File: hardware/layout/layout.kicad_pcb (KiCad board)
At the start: 4 copper layers, 60 parts, among them J1 ?, J2 ?, J3 2.54mm 18 x 2 SMD Vertical Fe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, SW1 ?, U1 ?, U2 ?, U3 ?, U4 ?, U5 ?, Y1 ECS-120-12-33Q-JES-TR

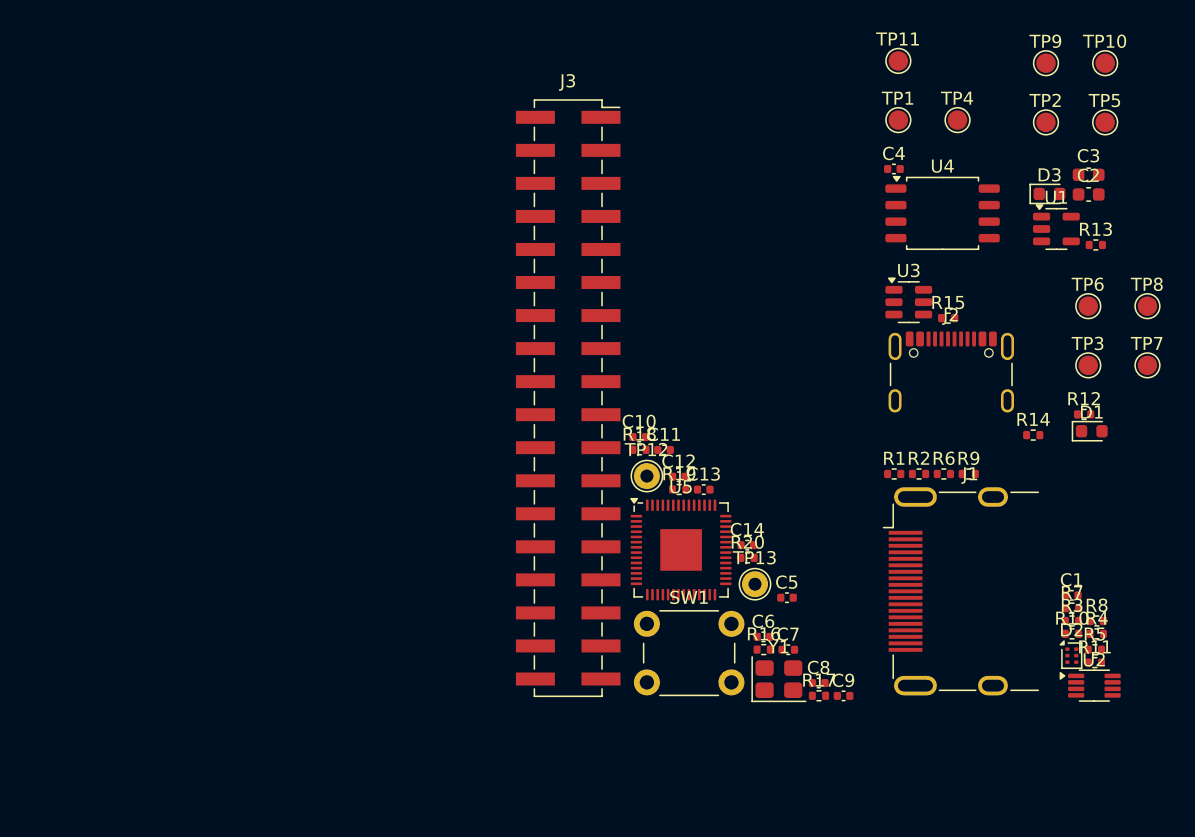
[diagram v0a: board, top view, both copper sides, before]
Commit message: hardware: DRC relaxation pass — 4-layer planes, pours, net classes, cost rules, clean silk
Checkpoint of the bring-up layout before the RP2040-module refactor.

- Planes/pours: In1=GND plane, In2=VDD_3V3 plane, F/B GND pours, GND
  stitch-via grid + QFN exposed-pad thermal vias.
- Resolved real DRC: track/pad clearances (incl. QSPI_IO3<->C7 via a
  small C7 nudge), dangling vias/tracks, starved thermals
  (min_resolved_spokes 2->1), isolated copper.
- Custom rules (layout.kicad_dru): 0.13mm fine-pitch clearance inside
  U2 (PCA9306) and U5 (RP2040 QFN) courtyards.
- Net classes: Power (VDD_*) 0.4mm, USB diff-pair 0.25/0.20mm.
- Project: resolve ${PCB_NAME}/${PCB_VERSION} title-block vars,
  lib_footprint_mismatch -> ignore.
- Silkscreen: hide all reference designators, strip body outlines to
  pin-1 / polarity marks only.
- Plus in-progress signal routing.

DRC: 0 error-severity violations; 38 unconnected remain (off-board
test-point stubs + unfinished on-board routing).
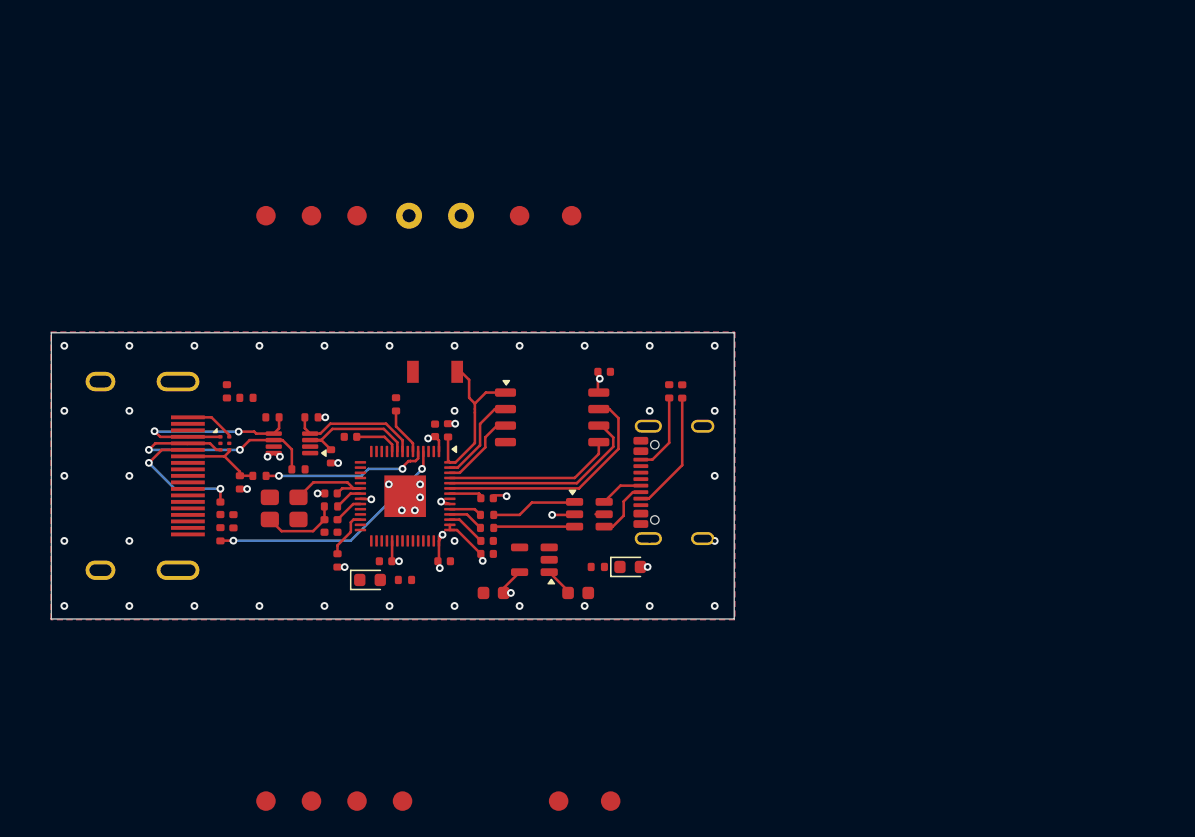
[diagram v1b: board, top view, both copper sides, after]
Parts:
- removed J3: 2.54mm 18 x 2 SMD Vertical Female, kicad_libraries_kicad-footprints_Connector_PinSocket_2.54mm@9.0.3:PinSocket_2x18_P2.54mm_Vertical_SMD
- D2: value ? -> PESD5V0L4UF
- J1: value ? -> 208658-1001
- J2: value ? -> USB4105-GF-A-060
- SW1: value ? -> B3U-1000P; footprint kicad_libraries_kicad-footprints_Button_Switch_THT@9.0.3:SW_PUSH_6mm -> kicad_libraries_kicad-footprints_Button_Switch_SMD@9.0.3:SW_SPST_B3U-1000P
- U2: value ? -> PCA9306DCTR
- U3: value ? -> USBLC6-2SC6
- U4: value ? -> W25Q16JVSSIQ
- moved TP10 80.8 mm to (123.5, 136.0)
- moved TP9 80.0 mm to (120.0, 136.0)
- moved TP8 77.7 mm to (116.5, 136.0)
- moved R5 69.6 mm to (113.5, 104.5), turned to 90 degrees
- moved TP11 68.5 mm to (127.0, 136.0)
- moved D2 67.1 mm to (113.3, 108.5)
- moved R4 66.9 mm to (114.0, 114.5), turned to -90 degrees
- moved R11 66.0 mm to (117.0, 106.5), turned to 180 degrees
- moved R3 65.8 mm to (113.0, 115.5), turned to 90 degrees
- moved C1 65.8 mm to (113.0, 113.5), turned to 90 degrees
- moved U2 64.4 mm to (118.5, 108.5), turned to 180 degrees
- moved J1 62.4 mm to (107.2, 111.0), turned to 180 degrees
- moved TP7 61.8 mm to (123.5, 91.0)
- moved TP5 61.4 mm to (120.0, 91.0)
- moved R10 60.8 mm to (119.0, 110.5)
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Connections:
- D2 pad 1: CEC_NODE -> DDC_SDA_5V
- D2 pad 3: HDMI._HPD -> DDC_SCL_5V
- D2 pad 4: DDC_SCL_5V -> CEC_NODE
- D2 pad 6: DDC_SDA_5V -> HDMI._HPD
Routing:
- net VDD_3V3: track 0.00 -> 25.0 mm, vias 0 -> 17
- net ARC_TX: track 0.00 -> 19.1 mm, vias 0 -> 2
- net DDC_SCL_5V: track 0.00 -> 19.1 mm, vias 0 -> 2
- net QSPI_IO3: track 0.00 -> 18.4 mm
- net QSPI_CLK: track 0.00 -> 15.9 mm
- net DDC_SDA_5V: track 0.00 -> 15.9 mm, vias 0 -> 2
- net QSPI_CS: track 0.00 -> 13.5 mm
- net QSPI_IO0: track 0.00 -> 13.1 mm
- net CEC_BUS: track 0.00 -> 12.9 mm, vias 0 -> 2
- net USB_D_N: track 0.00 -> 10.8 mm
- net HDMI._ARC14: track 0.00 -> 10.8 mm, vias 0 -> 2
- net DDC_SDA: track 0.00 -> 10.2 mm
- net DDC_SCL: track 0.00 -> 10.1 mm
- net USB_D_P: track 0.00 -> 9.97 mm
- net USBC.CC1: track 0.00 -> 9.40 mm
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- added copper zone on B.Cu, net GND
- added copper zone on F.Cu, net GND
- added copper zone on In1.Cu, net GND
- added copper zone on In2.Cu, net VDD_3V3
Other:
- board outline added: 52.5 x 22 mm

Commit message: hardware: shrink to 50x22mm, backside GPIO pads, DRC/netclass cleanup
- board outline 50.0x22.0mm: fits JLCPCB's cheap <=50x50 4-layer tier
- 14 backside expansion pads (1x1mm roundrect): GP17-22, GP26-29 (all
  4 ADC), 3V3/5V/GND; net-name silk labels instead of TP designators
- netclasses: drop *USB_D_* shadow pattern (pair now routes true 90R
  0.1867/0.127), RP_USB_D_* stubs into 90Ohm Diff, 50Ohm SE 0.2mm
- kicad_dru: retarget fine-pitch pad rule U2->U1 (refdes shuffle),
  add coupled diff-pair gap floor (0.125mm)
- JLC guards: min_hole_to_hole 0.254, min_through_hole 0.3, via
  presets trimmed to 0.5/0.3 + 0.6/0.3 (no surcharge drills)
- vias normalized: 0.6/0.3 power rails, 0.5/0.3 signal/GND (incl.
  fine-pitch fanout exceptions)
- full reroute; DRC clean: 0 violations, 0 unconnected
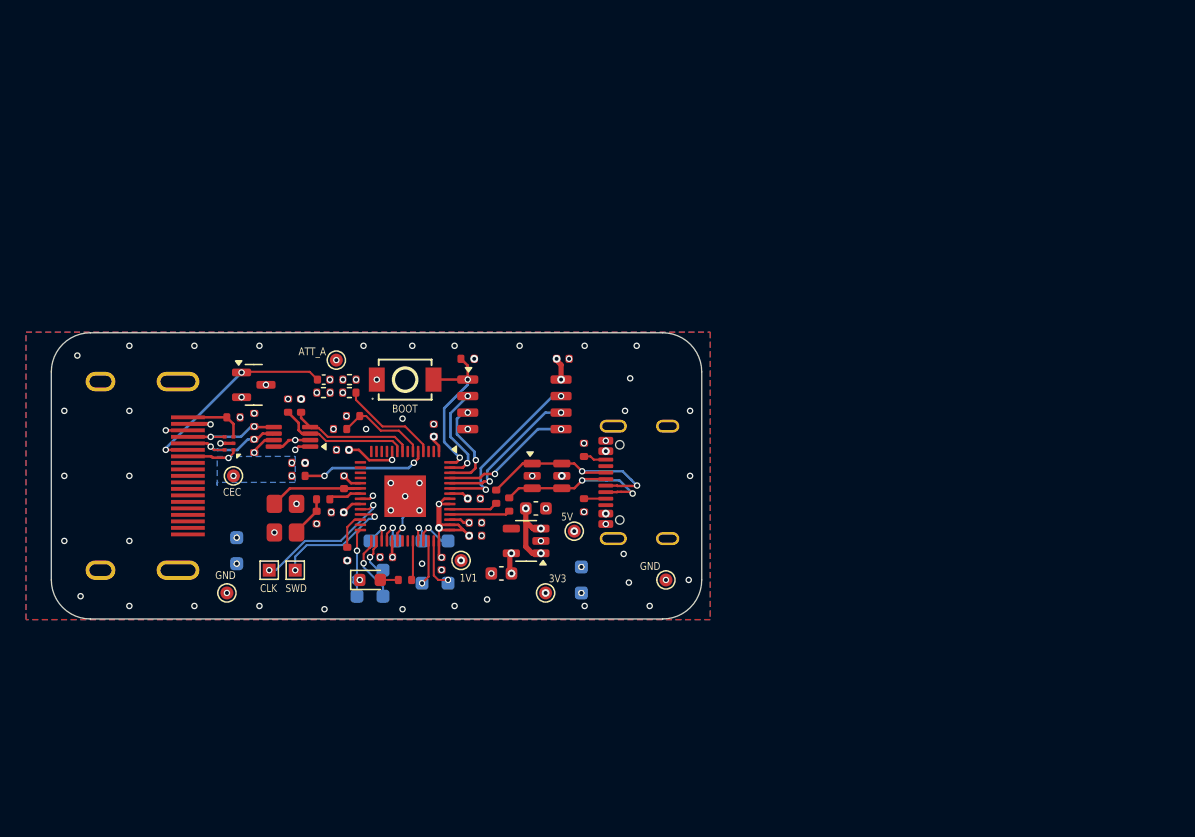
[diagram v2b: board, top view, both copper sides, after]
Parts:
- removed the R4 at (114.0, 114.5)
- removed the U1 at (137.1, 117.5)
- added R12: 0402WGF1000TCE, kicad_libraries_kicad-footprints_Resistor_SMD@9.0.3:R_0402_1005Metric, F.Cu at (122.9, 103.6)
- added TP14: ?, naorunaoru_picoarc_footprints_picoarc:TestPad_1.0x1.0mm_RoundRect, B.Cu at (130.5, 119.2)
- added TP15: ?, kicad_libraries_kicad-footprints_TestPoint@9.0.3:TestPoint_Pad_D1.0mm, F.Cu at (131.5, 117.5)
- added TP16: ?, kicad_libraries_kicad-footprints_TestPoint@9.0.3:TestPoint_Pad_D1.0mm, F.Cu at (138.0, 120.0)
- added TP17: ?, kicad_libraries_kicad-footprints_TestPoint@9.0.3:TestPoint_Pad_D1.0mm, F.Cu at (140.2, 115.2)
- added TP18: ?, kicad_libraries_kicad-footprints_TestPoint@9.0.3:TestPoint_Pad_D1.0mm, F.Cu at (121.9, 102.1)
- added TP19: ?, kicad_libraries_kicad-footprints_TestPoint@9.0.3:TestPoint_Pad_D1.0mm, F.Cu at (114.0, 111.0)
- added TP20: ?, kicad_libraries_kicad-footprints_TestPoint@9.0.3:TestPoint_Pad_D1.0mm, F.Cu at (147.2, 119.0)
- added TP21: ?, kicad_libraries_kicad-footprints_TestPoint@9.0.3:TestPoint_Pad_D1.0mm, F.Cu at (113.5, 120.0)
- added TP22: ?, kicad_libraries_kicad-footprints_TestPoint@9.0.3:TestPoint_Pad_1.0x1.0mm, F.Cu at (116.8, 118.2)
- added TP23: ?, kicad_libraries_kicad-footprints_TestPoint@9.0.3:TestPoint_Pad_1.0x1.0mm, F.Cu at (118.8, 118.2)
- added U2: AP2112K-3.3TRG1, kicad_libraries_kicad-footprints_Package_TO_SOT_SMD@9.0.3:SOT-23-5, F.Cu at (136.5, 116.0)
- C1: value GCM155R71H103KA55D -> CL05B103KB5NNNC
- C10, C11, C12, C4, C7, C8, C9: value GCM155R71H104KE02D -> CL05B104KB54PNC
- C13, C14: value GCM1555C1H150FA16D -> 0402CG150J500NT
- C2, C3: value GRM188Z71A106KA73D -> CL10A106MA8NRNC
- C5, C6: value GRM155Z71A105KE01D -> CL05A105KA5NQNC
- D1: value LED BLUE -> KT-0603R
- D3: value LED GREEN -> PESD5V0S2BT,215; footprint kicad_libraries_kicad-footprints_LED_SMD@9.0.3:LED_0603_1608Metric -> kicad_libraries_kicad-footprints_Package_TO_SOT_SMD@9.0.3:SOT-23
- R1: value ERJ-2RKF2702X -> 0402WGF2202TCE
- R10, R11, R8, R9: value ERJ-2RKF2201X -> 0402WGF2201TCE
- R13: value ERJ-2RKF2700X -> 0402WGF1200TCE
- R14, R15: value ERJ-2RKF5101X -> 0402WGF5101TCE
- R16, R17: value ERJ-2RKF1002X -> 0402WGF1002TCE
- R18, R19: value ERJ-2RKF27R0X -> 0402WGF330JTCE
- R2: value ERJ-2RKF2200X -> 0402WGF2200TCE
- R20, R5: value ERJ-2RKF1001X -> 0402WGF1001TCE
- R3: value ERJ-2RKF3300X -> 0402WGF3300TCE
- R4: renamed from R12; value ERJ-2RKF1001X -> 0402WGF1001TCE
- R6: value ERJ-2RKF6802X -> 0402WGF1003TCE
- R7: value ERJ-2RKF1003X -> 0402WGF1003TCE
- SW1: value B3U-1000P -> TS-1088-AR02016; footprint kicad_libraries_kicad-footprints_Button_Switch_SMD@9.0.3:SW_SPST_B3U-1000P -> naorunaoru_picoarc_footprints_picoarc:SW-SMD_L3.9-W3.0-P4.45
- TP1, TP10, TP11, TP2, TP3, TP4, TP5, TP6, TP7, TP8, TP9: footprint kicad_libraries_kicad-footprints_TestPoint@9.0.3:TestPoint_Pad_D1.5mm -> naorunaoru_picoarc_footprints_picoarc:TestPad_1.0x1.0mm_RoundRect; moved to B.Cu
- TP12, TP13: footprint kicad_libraries_kicad-footprints_TestPoint@9.0.3:TestPoint_THTPad_D2.0mm_Drill1.0mm -> naorunaoru_picoarc_footprints_picoarc:TestPad_1.0x1.0mm_RoundRect; moved to B.Cu
- U5: value ? -> RP2040
- Y1: value ECS-120-12-33Q-JES-TR -> X322512MSB4SI
- moved TP4 37.8 mm to (140.8, 120.0), turned to 180 degrees
- moved TP3 35.7 mm to (114.2, 115.8), turned to 180 degrees
- moved D3 32.1 mm to (115.6, 104.0)
- moved TP1 30.8 mm to (114.2, 117.8), turned to 180 degrees
- moved TP5 29.5 mm to (123.5, 120.2), turned to 180 degrees
- moved TP13 28.4 mm to (128.5, 119.2), turned to 180 degrees
- moved TP2 27.4 mm to (140.8, 118.0), turned to 180 degrees
- moved TP7 27.3 mm to (125.5, 118.2), turned to 180 degrees
- moved TP12 25.2 mm to (130.5, 116.0), turned to 180 degrees
- moved R13 25.0 mm to (120.9, 104.6)
- moved TP6 23.5 mm to (125.5, 120.2), turned to 180 degrees
- moved TP10 22.8 mm to (127.2, 113.5), turned to 180 degrees
- moved TP8 21.5 mm to (124.5, 116.0), turned to 180 degrees
- moved TP9 21.0 mm to (126.5, 116.0), turned to 180 degrees
- moved TP11 20.1 mm to (128.5, 116.0), turned to 180 degrees
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- renumbered U2 to U1
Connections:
- net GPIO0 renamed U_MCU.NC_GPIO0
- net GPIO1 renamed U_MCU.NC_GPIO1
- net GPIO10 renamed U_MCU.NC_GPIO10
- net GPIO11 renamed U_MCU.NC_GPIO11
- net GPIO12 renamed U_MCU.NC_GPIO12
- net GPIO13 renamed U_MCU.NC_GPIO13
- net GPIO14 renamed U_MCU.NC_GPIO14
- net GPIO15 renamed U_MCU.NC_GPIO15
- net GPIO16 renamed U_MCU.NC_GPIO16
- net GPIO23 renamed U_MCU.NC_GPIO23
- net GPIO24 renamed U_MCU.NC_GPIO24
- net GPIO5 renamed U_MCU.NC_GPIO5
- net GPIO8 renamed U_MCU.NC_GPIO8
- net GPIO9 renamed U_MCU.NC_GPIO9
- D2 pad 1: DDC_SDA_5V -> CEC_NODE
- D2 pad 3: DDC_SCL_5V -> HDMI._HPD
- D2 pad 4: CEC_NODE -> DDC_SDA_5V
- D2 pad 6: HDMI._HPD -> DDC_SCL_5V
- D3 pad 1: PWR.U1.LED_K -> HDMI._ARC14
- D3 pad 2: VDD_3V3 -> HDMI._HDMI_5V
- R13 pad 1: PWR.U1.LED_K -> ATT_A
- TP1 pad 1: VDD_1V1 -> VDD_3V3
- TP10 pad 1: DDC_SDA -> GP22
- TP11 pad 1: DDC_SDA_5V -> GP26
- TP12 pad 1: SWD_SWCLK -> GP27
- TP13 pad 1: SWD_SWDIO -> GP28
- TP2 pad 1: VDD_3V3 -> VDD_5V
- TP3 pad 1: VDD_5V -> GND
- TP4 pad 1: ATT_A -> GND
- TP5 pad 1: CEC_NODE -> GP17
- TP6 pad 1: GND -> GP18
- TP7 pad 1: GND -> GP19
- TP8 pad 1: DDC_SCL -> GP20
- TP9 pad 1: DDC_SCL_5V -> GP21
- U5 pad 28: GPIO17 -> GP17
- U5 pad 29: GPIO18 -> GP18
- U5 pad 30: GPIO19 -> GP19
- U5 pad 31: GPIO20 -> GP20
- U5 pad 32: GPIO21 -> GP21
- U5 pad 34: GPIO22 -> GP22
- U5 pad 38: GPIO26_ADC0 -> GP26
- U5 pad 39: GPIO27_ADC1 -> GP27
- U5 pad 40: GPIO28_ADC2 -> GP28
- U5 pad 41: GPIO29_ADC3 -> GP29
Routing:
- net ARC_TX: track 19.1 -> 7.69 mm, vias 2 -> 0
- net SWD_SWCLK: track 0.00 -> 11.3 mm, vias 0 -> 2
- net DDC_SCL_5V: track 19.1 -> 8.63 mm
- net SWD_SWDIO: track 0.00 -> 9.60 mm, vias 0 -> 2
- net DDC_SDA_5V: track 15.9 -> 8.03 mm
- net USBC.CC1: track 9.40 -> 1.68 mm
- net USB_D_P: track 9.97 -> 16.7 mm, vias 0 -> 2
- net GP17: track 0.00 -> 5.43 mm, vias 0 -> 1
- net HDMI._ARC14: track 10.8 -> 16.2 mm
- net QSPI_IO3: track 18.4 -> 13.1 mm, vias 0 -> 2
- net GP18: track 0.00 -> 5.11 mm, vias 0 -> 1
- net USBC.CC2: track 6.16 -> 1.78 mm
- net QSPI_CLK: track 15.9 -> 11.6 mm, vias 0 -> 2
- net GP29: track 0.00 -> 3.89 mm, vias 0 -> 1
- net HDMI._HDMI_5V: track 0.00 -> 3.85 mm, vias 0 -> 6
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- added copper zone on In1.Cu, net ATT_A
- added copper zone on B.Cu, net CEC_NODE
- added copper zone on In1.Cu, net HDMI._HDMI_5V
- added copper zone on In1.Cu, net VDD_1V1
- added copper zone on In1.Cu, net VDD_5V
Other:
- board size 52.5 x 22 mm -> 50 x 22 mm
- board text added: "1V1"
- board text added: "3V3"
- board text added: "5V"
- board text added: "ATT_A"
- board text added: "BOOT"
- board text added: "CEC"
- board text added: "CLK"
- board text added: "GND"
- board text added: "SWD"
